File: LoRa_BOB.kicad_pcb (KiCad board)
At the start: 4 copper layers, 22.9 x 59.7 mm, 8 parts, among them U1 1597-1488-ND, U2 XC6210B332MR-G, U3 74HC4050D

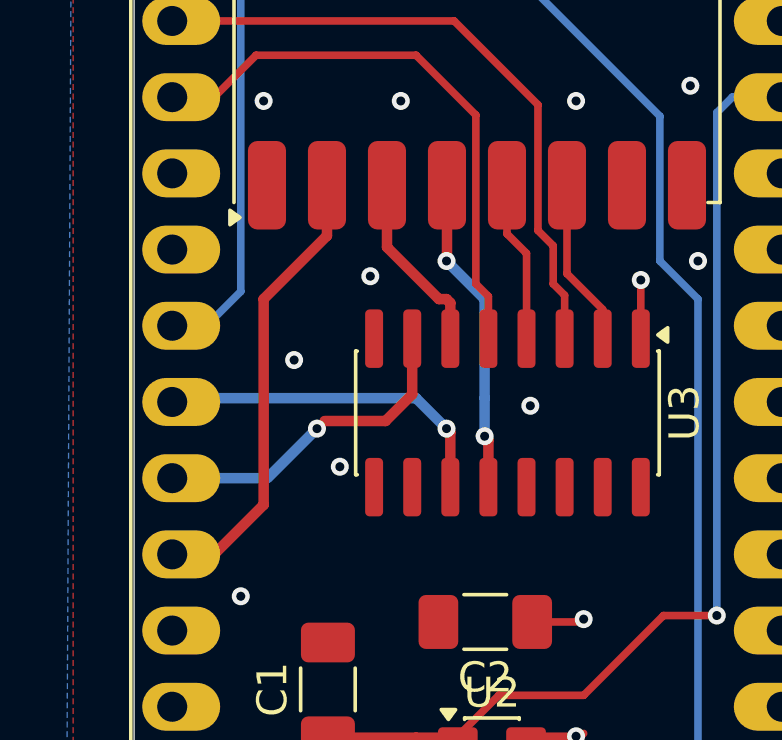
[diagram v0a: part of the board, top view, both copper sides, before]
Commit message: Better netclasses and 50 ohm trace widths
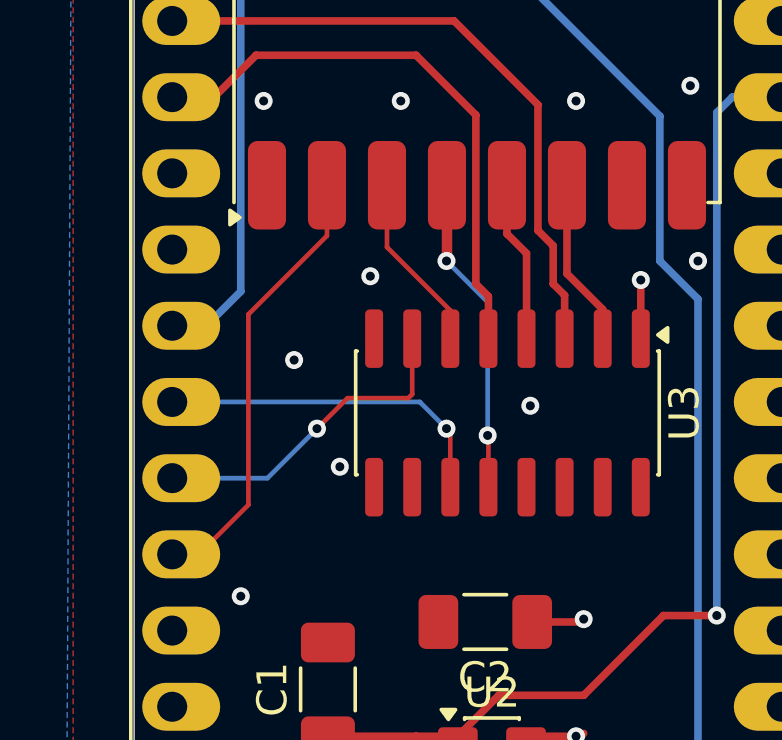
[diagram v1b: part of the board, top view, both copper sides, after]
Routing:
- net /MISO: track 15.3 -> 17.5 mm
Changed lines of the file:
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@@
 			(net 45 "unconnected-(U1-DIO5-Pad7)")
 			(pinfunction "DIO5")
-			(pintype "bidirectional")
+			(pintype "bidirectional+no_connect")
 		)
 		(pad "8" smd roundrect
@@
 			(net 47 "unconnected-(U1-DIO3-Pad11)")
 			(pinfunction "DIO3")
-			(pintype "bidirectional")
+			(pintype "bidirectional+no_connect")
 		)
 		(pad "12" smd roundrect
@@
 			(net 43 "unconnected-(U1-DIO4-Pad12)")
 			(pinfunction "DIO4")
-			(pintype "bidirectional")
+			(pintype "bidirectional+no_connect")
 		)
 		(pad "13" smd roundrect
@@
 			(net 48 "unconnected-(U1-DIO2-Pad16)")
 			(pinfunction "DIO2")
-			(pintype "bidirectional")
+			(pintype "bidirectional+no_connect")
 		)
 		(embedded_fonts no)
@@
 			(net 42 "unconnected-(U3-4A-Pad9)")
 			(pinfunction "4A")
-			(pintype "input")
+			(pintype "input+no_connect")
 		)
 		(pad "10" smd roundrect
@@
 			(net 37 "unconnected-(U3-4Y-Pad10)")
 			(pinfunction "4Y")
-			(pintype "output")
+			(pintype "output+no_connect")
 		)
 		(pad "11" smd roundrect
@@
 			(net 31 "unconnected-(U3-6A-Pad14)")
 			(pinfunction "6A")
-			(pintype "input")
+			(pintype "input+no_connect")
 		)
 		(pad "15" smd roundrect
@@
 			(net 38 "unconnected-(U3-6Y-Pad15)")
 			(pinfunction "6Y")
-			(pintype "output")
+			(pintype "output+no_connect")
 		)
 		(pad "16" smd roundrect
@@
 	)
 	(segment
-		(start 205.994 134.366)
-		(end 206.882353 133.477647)
-		(width 0.35)
+		(start 206.882353 131.62111)
+		(end 206.882353 133.476353)
+		(width 0.156)
 		(layer "F.Cu")
 		(net 32)
 	)
 	(segment
-		(start 206.882353 133.477647)
-		(end 206.882353 131.62111)
-		(width 0.35)
+		(start 204.724 133.604)
+		(end 206.754706 133.604)
+		(width 0.156)
 		(layer "F.Cu")
 		(net 32)
 	)
 	(segment
-		(start 203.962 134.366)
-		(end 205.994 134.366)
-		(width 0.35)
+		(start 203.708 134.62)
+		(end 204.724 133.604)
+		(width 0.156)
+		(layer "F.Cu")
+		(net 32)
+	)
+	(segment
+		(start 206.882353 133.476353)
+		(end 206.754706 133.604)
+		(width 0.156)
 		(layer "F.Cu")
 		(net 32)
@@
 	)
 	(segment
-		(start 201.93 136.271)
-		(end 198.882 136.271)
-		(width 0.35)
+		(start 202.057 136.271)
+		(end 203.708 134.62)
+		(width 0.156)
 		(layer "B.Cu")
 		(net 32)
 	)
 	(segment
-		(start 203.708 134.62)
+		(start 198.882 136.271)
 		(end 202.057 136.271)
-		(width 0.35)
+		(width 0.156)
 		(layer "B.Cu")
 		(net 32)
@@
 	)
 	(segment
-		(start 208.041328 126.507465)
-		(end 208.041328 129.016672)
-		(width 0.35)
-		(layer "F.Cu")
-		(net 33)
-	)
-	(segment
 		(start 209.422353 136.57111)
 		(end 209.422353 135.000353)
-		(width 0.35)
+		(width 0.156)
 		(layer "F.Cu")
 		(net 33)
@@
 		(start 209.422353 135.000353)
 		(end 209.296 134.874)
+		(width 0.156)
+		(layer "F.Cu")
+		(net 33)
+	)
+	(segment
+		(start 208.041328 126.507465)
+		(end 208.041328 129.016672)
 		(width 0.35)
 		(layer "F.Cu")
@@
 	)
 	(via
-		(at 209.296 134.874)
+		(at 209.397305 134.847731)
 		(size 0.6)
 		(drill 0.3)
@@
 	)
 	(segment
-		(start 209.296 133.604)
-		(end 209.296 134.874)
-		(width 0.35)
-		(layer "B.Cu")
-		(net 33)
-	)
-	(segment
-		(start 209.296 130.302)
-		(end 209.296 133.604)
-		(width 0.35)
+		(start 209.397305 130.403305)
+		(end 208.026 129.032)
+		(width 0.156)
 		(layer "B.Cu")
 		(net 33)
 	)
 	(segment
-		(start 208.026 129.032)
-		(end 209.296 130.302)
-		(width 0.35)
+		(start 209.397305 134.847731)
+		(end 209.397305 130.403305)
+		(width 0.156)
 		(layer "B.Cu")
 		(net 33)
@@
 	)
 	(segment
-		(start 208.026 130.302)
-		(end 207.772 130.302)
-		(width 0.35)
-		(layer "F.Cu")
-		(net 35)
-	)
-	(segment
-		(start 207.772 130.302)
-		(end 206.041328 128.571328)
-		(width 0.35)
-		(layer "F.Cu")
-		(net 35)
-	)
-	(segment
 		(start 208.152353 131.62111)
-		(end 208.152353 130.428353)
-		(width 0.35)
+		(end 208.152353 130.682353)
+		(width 0.156)
 		(layer "F.Cu")
 		(net 35)
 	)
 	(segment
-		(start 208.152353 130.428353)
-		(end 208.026 130.302)
-		(width 0.35)
+		(start 206.041328 128.571328)
+		(end 206.041328 126.507465)
+		(width 0.156)
 		(layer "F.Cu")
 		(net 35)
 	)
 	(segment
-		(start 206.041328 128.571328)
-		(end 206.041328 126.507465)
-		(width 0.35)
+		(start 208.152353 130.682353)
+		(end 206.041328 128.571328)
+		(width 0.156)
 		(layer "F.Cu")
 		(net 35)
@@
 	)
 	(segment
-		(start 208.152353 136.57111)
-		(end 208.152353 134.746353)
-		(width 0.35)
+		(start 208.152353 134.746353)
+		(end 208.152353 136.57111)
+		(width 0.156)
 		(layer "F.Cu")
 		(net 41)
 	)
 	(segment
-		(start 208.152353 134.746353)
-		(end 208.026 134.62)
-		(width 0.35)
+		(start 208.026 134.62)
+		(end 208.152353 134.746353)
+		(width 0.156)
 		(layer "F.Cu")
 		(net 41)
@@
 	)
 	(segment
-		(start 207.01 133.604)
-		(end 208.026 134.62)
+		(start 198.882 133.731)
+		(end 199.009 133.604)
 		(width 0.35)
 		(layer "B.Cu")
@@
 	(segment
 		(start 198.882 133.731)
-		(end 199.009 133.604)
-		(width 0.35)
+		(end 207.137 133.731)
+		(width 0.156)
 		(layer "B.Cu")
 		(net 41)
 	)
 	(segment
-		(start 199.009 133.604)
-		(end 207.01 133.604)
-		(width 0.35)
+		(start 207.137 133.731)
+		(end 208.026 134.62)
+		(width 0.156)
 		(layer "B.Cu")
 		(net 41)
@@
 	)
 	(segment
-		(start 204.041328 128.190672)
-		(end 204.041328 126.507465)
+		(start 200.025 138.811)
+		(end 198.882 138.811)
 		(width 0.35)
 		(layer "F.Cu")
@@
 	)
 	(segment
-		(start 201.93 137.16)
-		(end 201.93 130.302)
-		(width 0.35)
+		(start 201.422 130.81)
+		(end 201.422 137.16)
+		(width 0.156)
 		(layer "F.Cu")
 		(net 46)
 	)
 	(segment
-		(start 201.93 130.302)
+		(start 204.041328 128.190672)
+		(end 201.422 130.81)
+		(width 0.156)
+		(layer "F.Cu")
+		(net 46)
+	)
+	(segment
+		(start 199.771 138.811)
+		(end 198.882 138.811)
+		(width 0.156)
+		(layer "F.Cu")
+		(net 46)
+	)
+	(segment
+		(start 204.041328 126.507465)
 		(end 204.041328 128.190672)
-		(width 0.35)
+		(width 0.156)
 		(layer "F.Cu")
 		(net 46)
 	)
 	(segment
-		(start 200.279 138.811)
-		(end 201.93 137.16)
-		(width 0.35)
+		(start 201.422 137.16)
+		(end 199.771 138.811)
+		(width 0.156)
 		(layer "F.Cu")
 		(net 46)

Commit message: LEDs
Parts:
- added D1: LED, LED_SMD:LED_0603_1608Metric_Pad1.05x0.95mm_HandSolder, F.Cu at (241.4, 110.5)
- added D2: SML-D12D8WT86, LED_SMD:LED_0603_1608Metric_Pad1.05x0.95mm_HandSolder, F.Cu at (241.4, 113.0)
- added D3: LED, LED_SMD:LED_0603_1608Metric_Pad1.05x0.95mm_HandSolder, F.Cu at (241.4, 115.6)
- added R1: 1K, Resistor_SMD:R_0201_0603Metric_Pad0.64x0.40mm_HandSolder, F.Cu at (244.9, 110.0)
- added R2: 1K, Resistor_SMD:R_0201_0603Metric_Pad0.64x0.40mm_HandSolder, F.Cu at (244.9, 111.8)
- added R3: 1K, Resistor_SMD:R_0201_0603Metric_Pad0.64x0.40mm_HandSolder, F.Cu at (244.9, 113.5)
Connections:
- net Net-(AE1-A) renamed /ANT
- A1 pad 19: unconnected-(A1-D5-Pad19) -> /ORANGE
- A1 pad 20: unconnected-(A1-D6-Pad20) -> /YELLOW
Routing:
- net /MISO: track 17.5 -> 18.2 mm

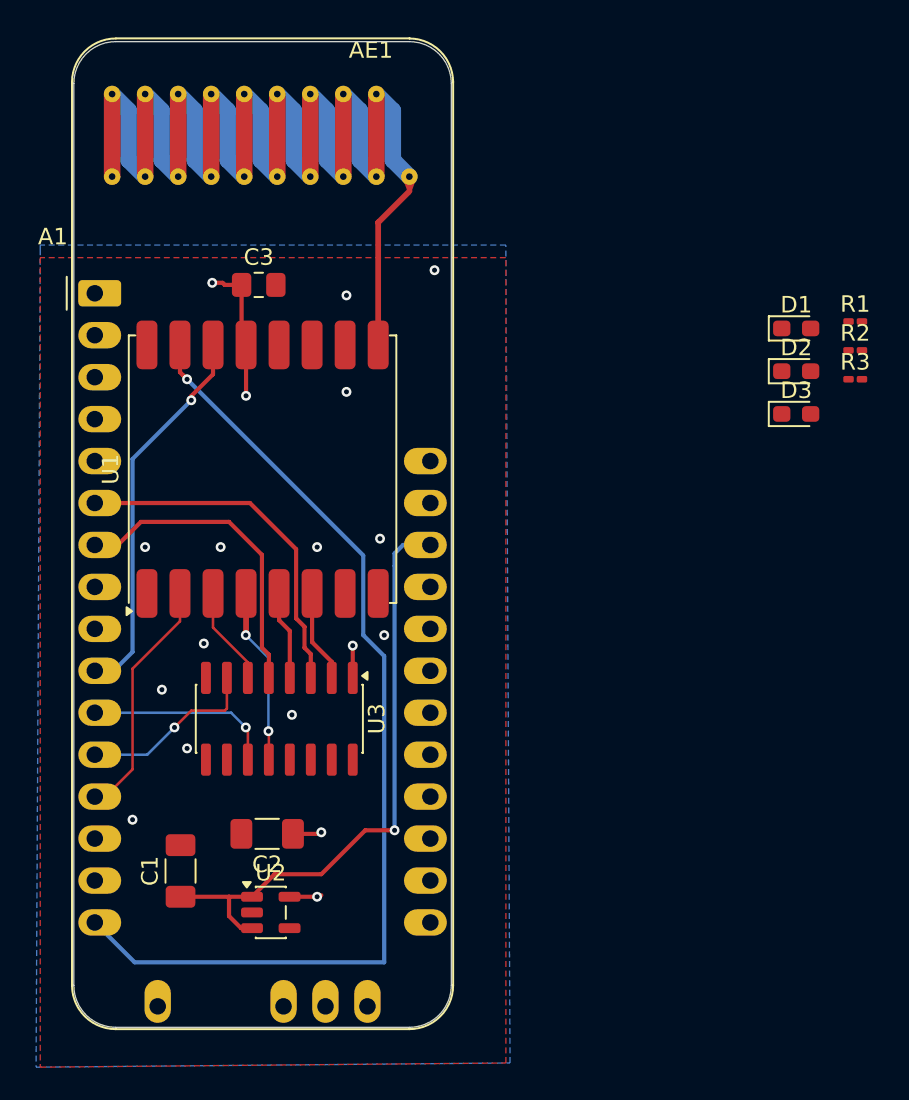
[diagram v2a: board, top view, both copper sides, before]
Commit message: LEDs were placed on PCB
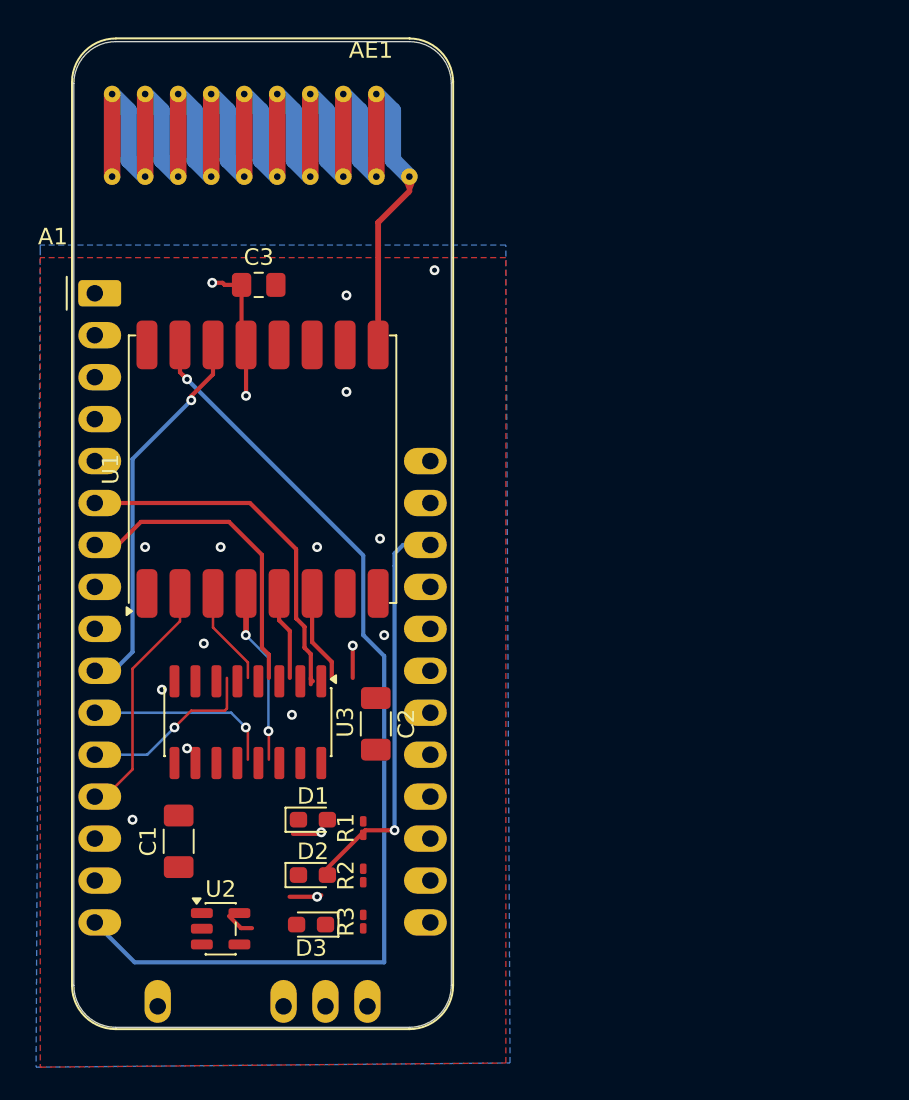
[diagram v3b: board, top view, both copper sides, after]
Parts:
- moved R3 44.3 mm to (215.1, 146.4), turned to 90 degrees
- moved R2 43.6 mm to (215.1, 143.6), turned to 90 degrees
- moved R1 42.8 mm to (215.1, 140.7), turned to 90 degrees
- moved D3 42.7 mm to (212.0, 146.6), turned to 180 degrees
- moved D2 42.3 mm to (212.1, 143.6)
- moved D1 41.7 mm to (212.1, 140.2)
- moved C2 9.36 mm to (215.9, 134.4), turned to -90 degrees
- moved U2 3.19 mm to (206.5, 146.8)
- moved U3 1.92 mm to (208.2, 134.3)
- moved C1 1.80 mm to (204.0, 141.5)
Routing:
- net Net-(A1-USB): track 36.6 -> 24.7 mm
- net /YELLOW: track 0.00 -> 1.96 mm, vias 0 -> 1
- net +3V3: track 14.5 -> 14.3 mm, vias 5 -> 4

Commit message: R's are 0603
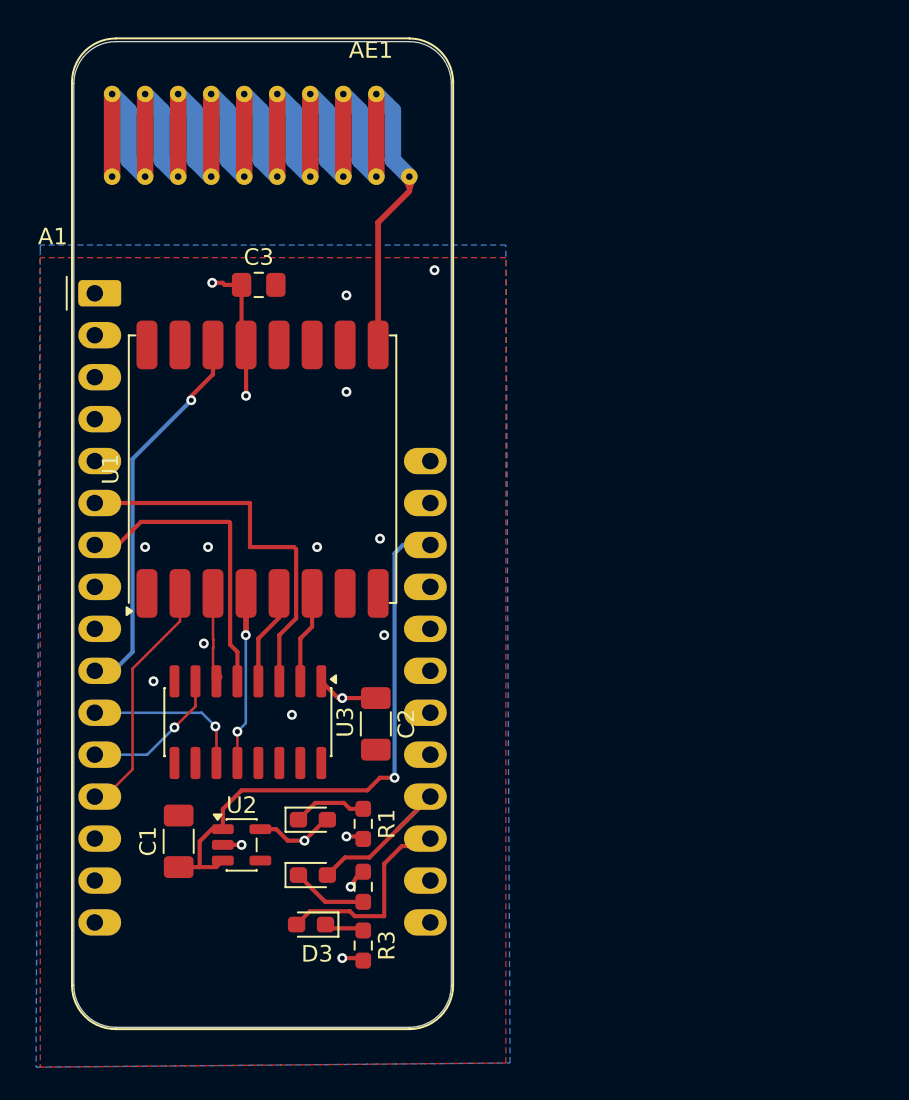
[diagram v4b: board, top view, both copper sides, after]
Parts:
- D1: value LED -> LTST_C-192KRKT-5A Red
- D2: value SML-D12D8WT86 -> LTST-C193KFKT-5A Yellow
- D3: value LED -> LTST-C192KGKT-5A Yellow-Green
- R1, R2, R3: value 1K -> 500; footprint Resistor_SMD:R_0201_0603Metric_Pad0.64x0.40mm_HandSolder -> Resistor_SMD:R_0603_1608Metric_Pad0.98x0.95mm_HandSolder
- moved U2 5.24 mm to (207.8, 141.7)
- moved R3 1.45 mm to (215.1, 147.8), turned to -90 degrees
- moved R2 0.69 mm to (215.1, 144.3)
- moved R1 0.25 mm to (215.1, 140.5), turned to -90 degrees
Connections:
- A1 pad 16: Net-(A1-DIO1) -> unconnected-(A1-DIO1-Pad16)
- A1 pad 19: /ORANGE -> /GREEN
- D2 pad 2: /ORANGE -> /YELLOW
- D3 pad 2: /YELLOW -> /GREEN
- U1 pad 15: Net-(A1-DIO1) -> unconnected-(U1-DIO1-Pad15)
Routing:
- net Net-(A1-DIO1): track 61.4 -> 0.00 mm, vias 1 -> 0
- net /GREEN: track 0.00 -> 12.2 mm
- net /YELLOW: track 1.96 -> 12.7 mm, vias 1 -> 0
- net Net-(A1-USB): track 24.7 -> 34.5 mm
- net GND: track 0.00 -> 5.18 mm, vias 13 -> 15
- net Net-(D2-K): track 0.00 -> 4.60 mm
- net Net-(D1-K): track 0.00 -> 4.49 mm
- net +3V3: track 14.3 -> 17.3 mm
- net Net-(D3-K): track 0.00 -> 2.38 mm
- net /MOSI: track 11.0 -> 8.83 mm
- net /SCK: track 11.7 -> 9.83 mm
- net /~{RESET}: track 22.1 -> 23.3 mm
- net unconnected-(A1-DIO1-Pad16): track 0.00 -> 0.72 mm
- net /CS: track 19.2 -> 18.6 mm
- net /SCK_3V: track 10.7 -> 10.2 mm

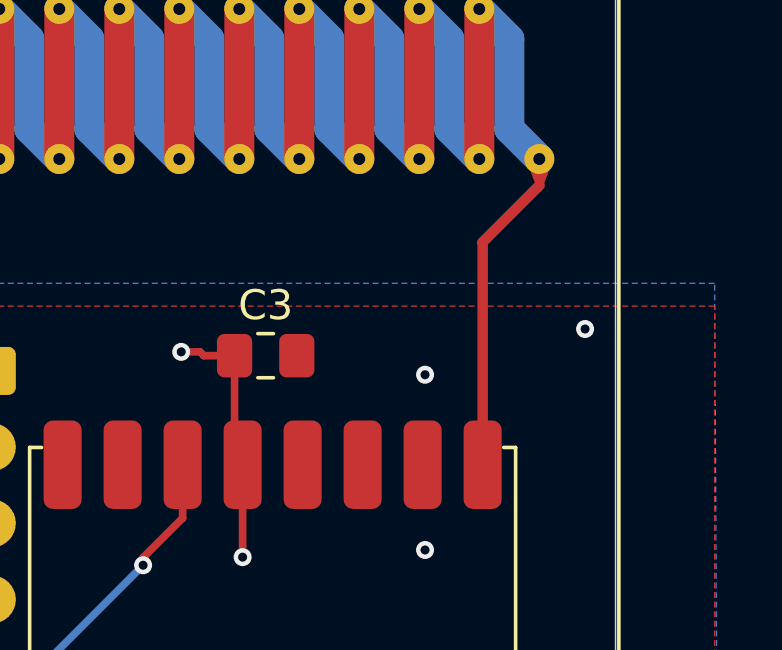
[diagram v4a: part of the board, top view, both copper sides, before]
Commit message: Added Antenna Matching L and C
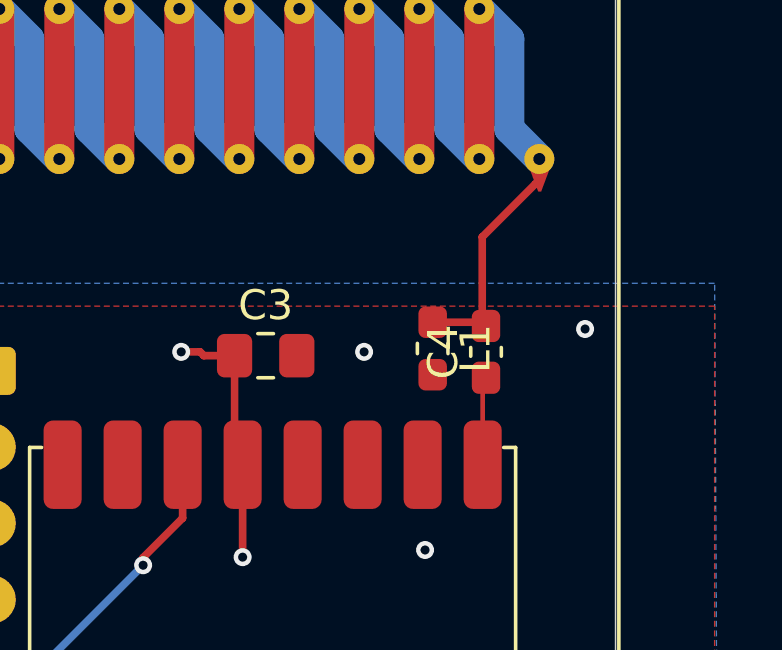
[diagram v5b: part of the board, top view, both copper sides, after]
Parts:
- added C4: 1p, Capacitor_SMD:C_0603_1608Metric_Pad1.08x0.95mm_HandSolder, F.Cu at (216.2, 107.7)
- added L1: 12n, Inductor_SMD:L_0603_1608Metric_Pad1.05x0.95mm_HandSolder, F.Cu at (214.4, 107.6)
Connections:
- AE1 pad 1: /ANT -> Net-(AE1-A)
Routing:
- net Net-(AE1-A): track 0.00 -> 7.32 mm
- net /ANT: track 10.1 -> 2.95 mm
